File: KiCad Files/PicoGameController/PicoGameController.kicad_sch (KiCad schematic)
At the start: 26 parts, among them J1 USB_OTG, J2 Conn_01x02, U1 RP2040, U2 NCP1117-3.3_SOT223, U3 W25Q128JVS, Y1 ABLS-12.000MHZ-B4-T

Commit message: Adding lots of buttons
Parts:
- added C17, C18, C19, C20: 1uF, symbol Device:C
- added R2, R6, R7, R8: 10k, symbol Device:R
- added SW1, SW10, SW11, SW12, SW13, SW2, SW3, SW4, SW5, SW6, SW7, SW8, SW9: SW_SPST, symbol Switch:SW_SPST
- added T1, T2: THB001P, symbol CustomParts:THB001P
- added U4, U5: DRV2605LDGS, Package_SO:VSSOP-10_3x3mm_P0.5mm, symbol Driver_Haptic:DRV2605LDGS
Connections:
- net GND: now also U1.57 (GND), C17.2, C18.1, C19.2, C20.2, SW1.2 (B), SW10.2 (B), SW11.2 (B), SW12.2 (B), SW13.2 (B), SW2.2 (B), SW3.2 (B), SW4.2 (B), SW5.2 (B), SW6.2 (B), SW7.2 (B), SW8.2 (B), SW9.2 (B), T1.1 (GND), T1.4 (GND), T1.7 (GND), T2.1 (GND), T2.4 (GND), T2.7 (GND), U4.8 (GND), U5.8 (GND)
- net QSPI_SCLK: now also U1.52 (QSPI_SCLK)
- net QSPI_SD0: now also U1.53 (QSPI_SD0)
- net QSPI_SD1: now also U1.55 (QSPI_SD1)
- net QSPI_SD2: now also U1.54 (QSPI_SD2)
- net QSPI_SD3: now also U1.51 (QSPI_SD3)
- net QSPI_SS: now also U1.56 (QSPI_SS)
- net XIN: now also U1.20 (XIN)
- net XOUT: now also U1.21 (XOUT)
- net LOGO: now reaches U1.14 (GPIO11)
- net LOGO: now also SW11.1 (A)
- net START: now reaches U1.15 (GPIO12)
- net START: now also SW3.1 (A)
- net SELECT: now reaches U1.16 (GPIO13)
- net SELECT: now also SW4.1 (A)
- net R1: now reaches U1.17 (GPIO14)
- net R1: now also SW7.1 (A)
- net L1: now reaches U1.18 (GPIO15)
- net L1: now also SW8.1 (A)
- net HAPTIC_L_SDA: now reaches U1.2 (GPIO0)
- net HAPTIC_L_SDA: now also R2.1
- net Y: now reaches U1.27 (GPIO16)
- net Y: now also SW13.1 (A)
- net X: now reaches U1.28 (GPIO17)
- net X: now also SW12.1 (A)
- net D_Up: now reaches U1.29 (GPIO18)
- net D_Up: now also SW1.1 (A)
- net HAPTIC_L_SCL: now reaches U1.3 (GPIO1)
- net HAPTIC_L_SCL: now also R6.1
- net D_Right: now reaches U1.30 (GPIO19)
- net D_Right: now also SW6.1 (A)
- net D_Left: now reaches U1.31 (GPIO20)
- net D_Left: now also SW5.1 (A)
- net D_Down: now reaches U1.32 (GPIO21)
- net D_Down: now also SW2.1 (A)
- net B: now reaches U1.34 (GPIO22)
- net B: now also SW10.1 (A)
- net A: now reaches U1.35 (GPIO23)
- net A: now also SW9.1 (A)
- net R3: now reaches U1.36 (GPIO24)
- net R3: now also T2.8 (Select)
- net L3: now reaches U1.37 (GPIO25)
- net L3: now also T1.8 (Select)
- net Lx: now reaches U1.38 (GPIO26_ADC0)
- net Lx: now also T1.3 (X)
- net Ly: now reaches U1.39 (GPIO27_ADC1)
- net Ly: now also T1.6 (Y)
- net HAPTIC_R_SDA: now reaches U1.4 (GPIO2)
- net HAPTIC_R_SDA: now also R7.1
- net Rx: now reaches U1.40 (GPIO28_ADC2)
- net Rx: now also T2.3 (X)
- net Ry: now reaches U1.41 (GPIO29_ADC3)
- net Ry: now also T2.6 (Y)
- net HAPTIC_R_SCL: now reaches U1.5 (GPIO3)
- net HAPTIC_R_SCL: now also R8.1
- new net: R8.2, U5.2 (SCL)
- new net: R6.2, U4.2 (SCL)
- new net: R7.2, U5.3 (SDA)
- new net: C19.1, U4.1 (REG)
- new net: R2.2, U4.3 (SDA)
- new net: C20.1, U5.1 (REG)
- new net +5V: C17.1, C18.2, T1.2 (VCC), T1.5 (VCC), T2.2 (VCC), T2.5 (VCC), U4.10 (VDD), U4.5 (EN), U5.10 (VDD), U5.5 (EN)
- no-connect marks 1 -> 5
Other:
- moved on the sheet: C2, C3, C5, J2, R1, R5, U3, Y1

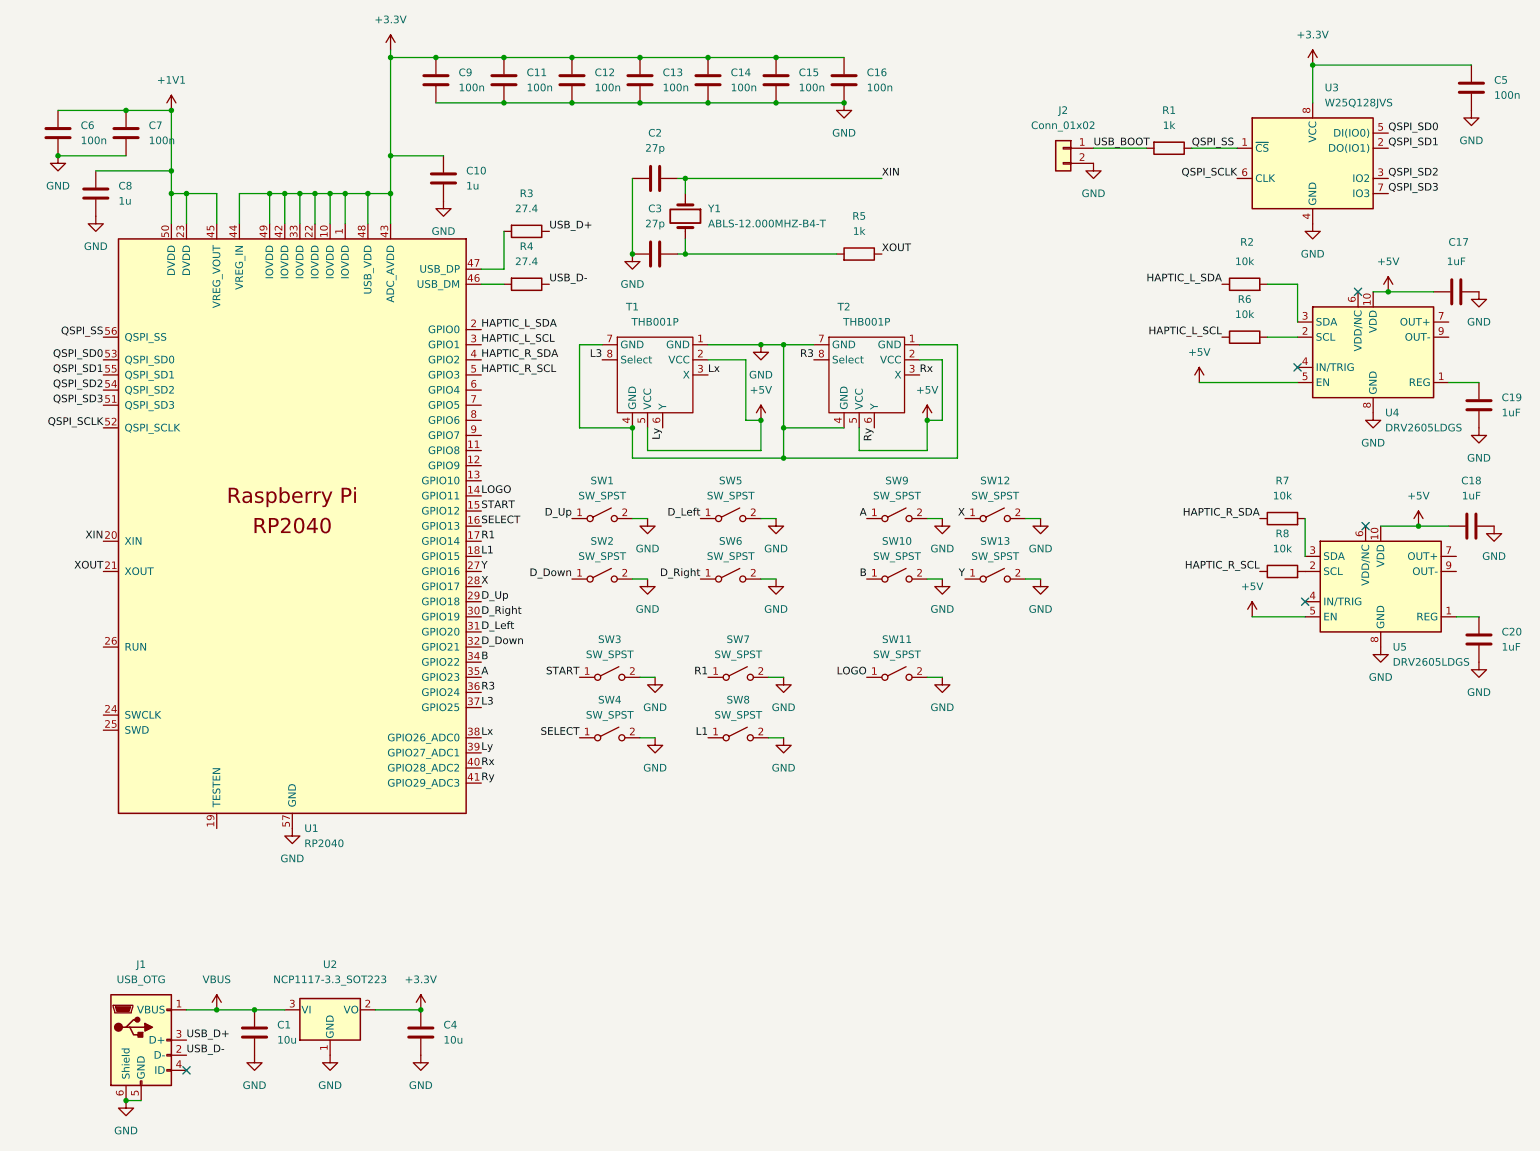
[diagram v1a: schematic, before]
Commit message: adding more ADCs
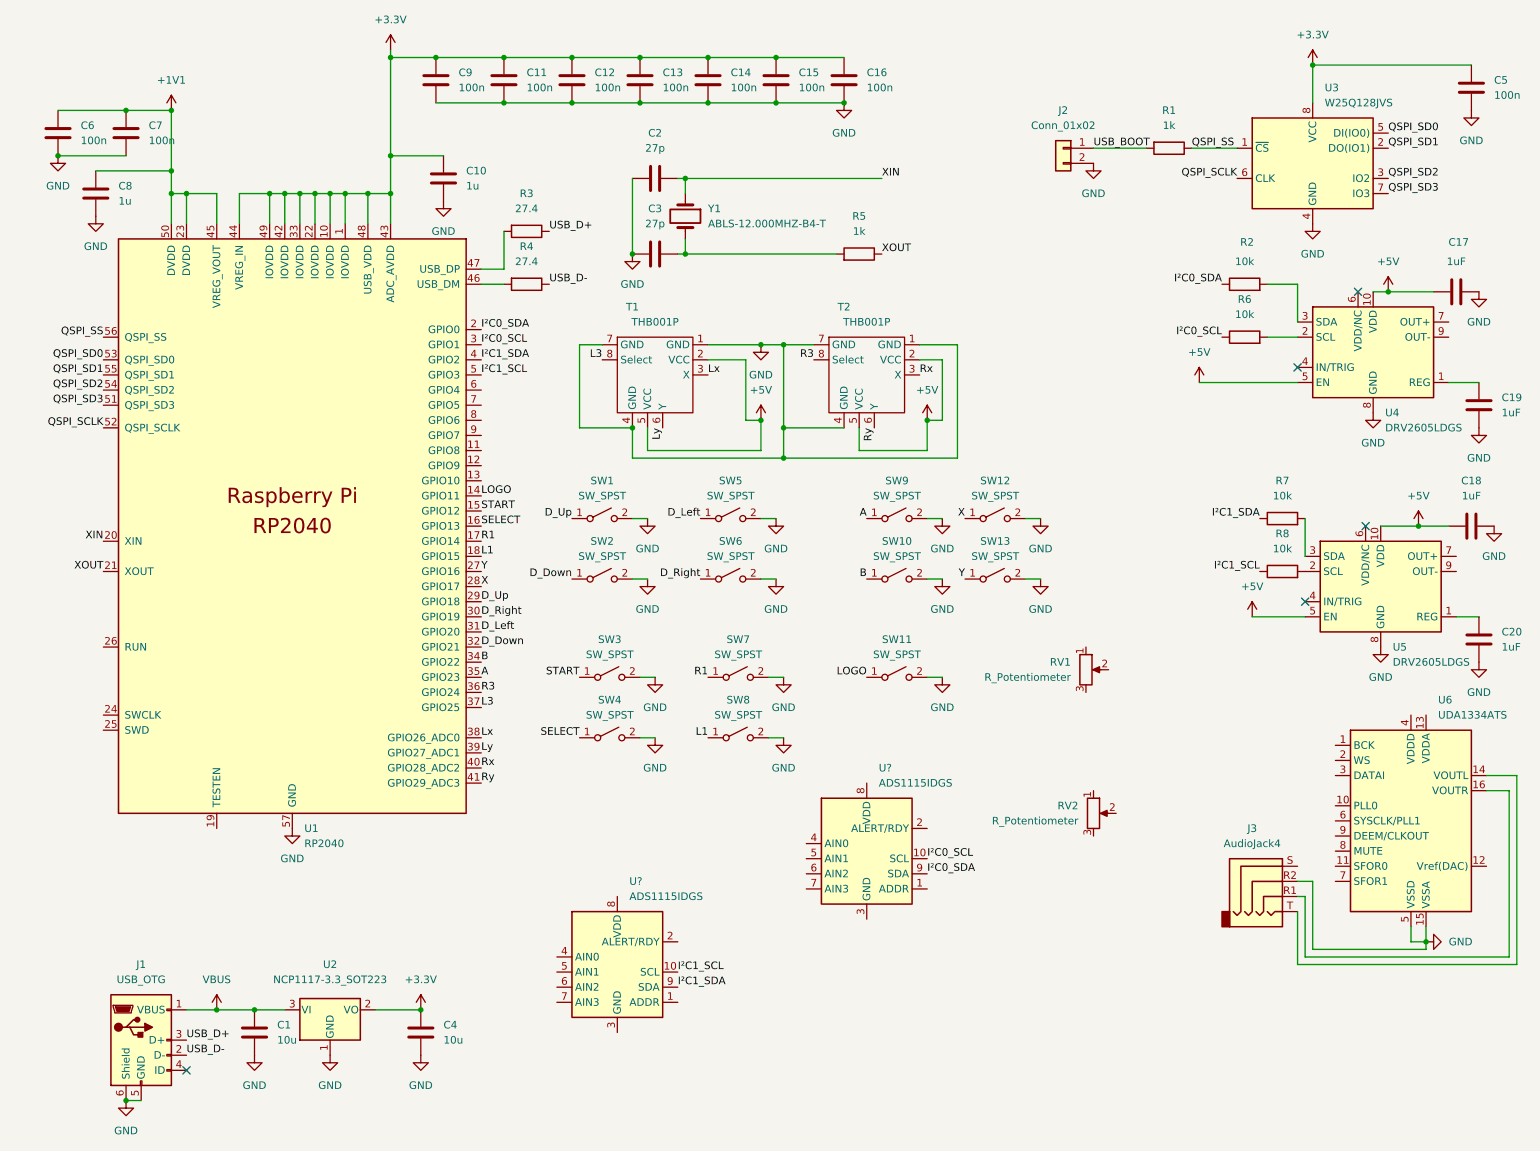
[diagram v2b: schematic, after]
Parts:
- added J3: AudioJack4, symbol Connector:AudioJack4
- added RV1, RV2: R_Potentiometer, symbol Device:R_Potentiometer
- added U6: UDA1334ATS, Package_SO:SSOP-16_4.4x5.2mm_P0.65mm, symbol Audio:UDA1334ATS
- added U? (x2): ADS1115IDGS, Package_SO:TSSOP-10_3x3mm_P0.5mm, symbol Analog_ADC:ADS1115IDGS
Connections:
- net GND: now also J3.R2, U6.15 (VSSA), U6.5 (VSSD)
- net HAPTIC_L_SCL renamed I²C0_SCL
- net I²C0_SCL: now also U?.10 (SCL)
- net HAPTIC_L_SDA renamed I²C0_SDA
- net I²C0_SDA: now also U?.9 (SDA)
- net HAPTIC_R_SCL renamed I²C1_SCL
- net I²C1_SCL: now also U?.10 (SCL)
- net HAPTIC_R_SDA renamed I²C1_SDA
- net I²C1_SDA: now also U?.9 (SDA)
- new net: J3.R1, U6.16 (VOUTR)
- new net: J3.T, U6.14 (VOUTL)

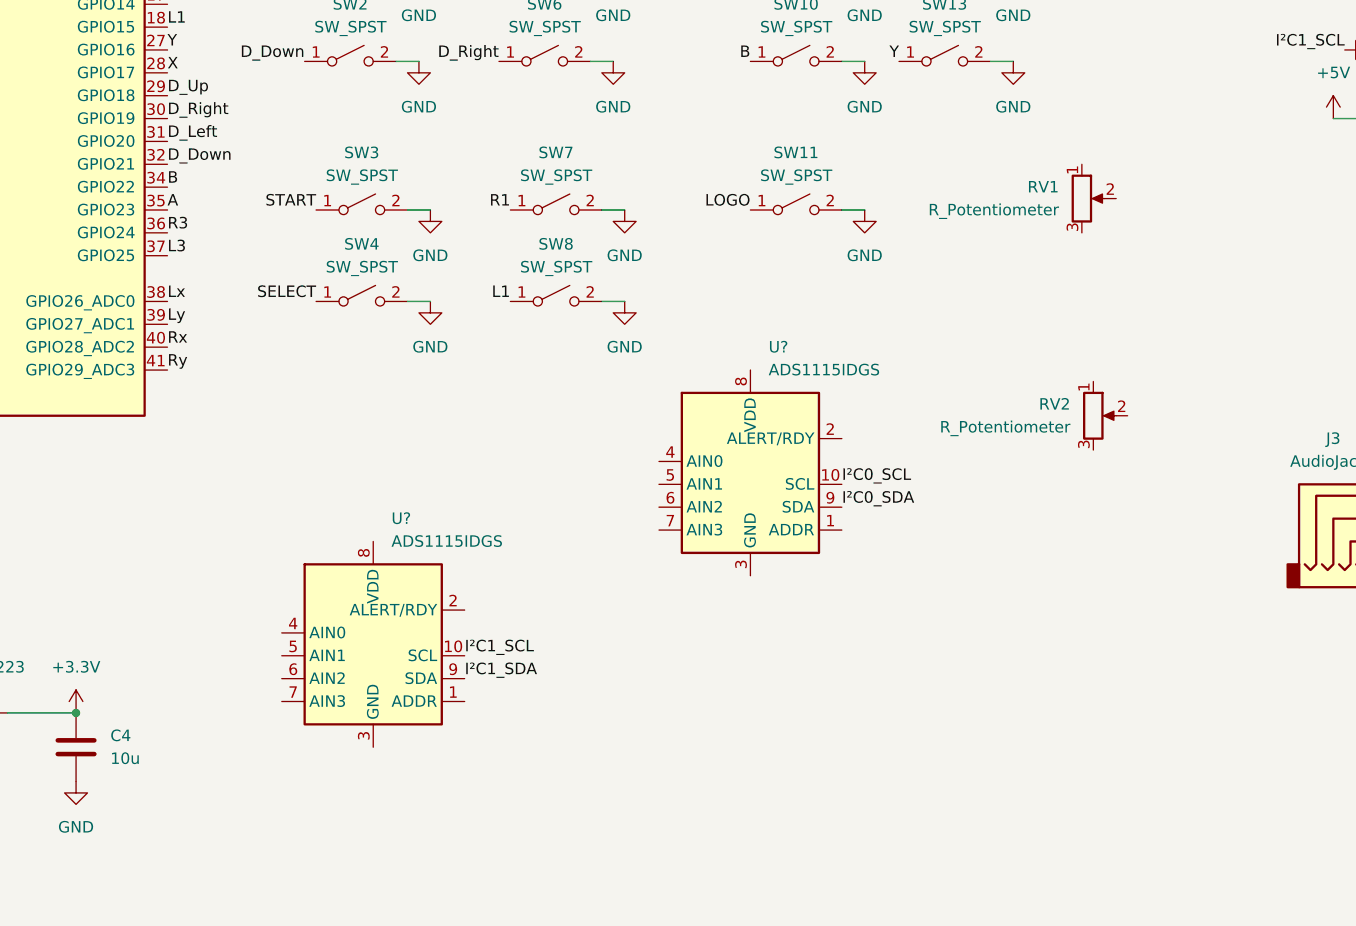
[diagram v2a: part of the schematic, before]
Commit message: Adding part footprints
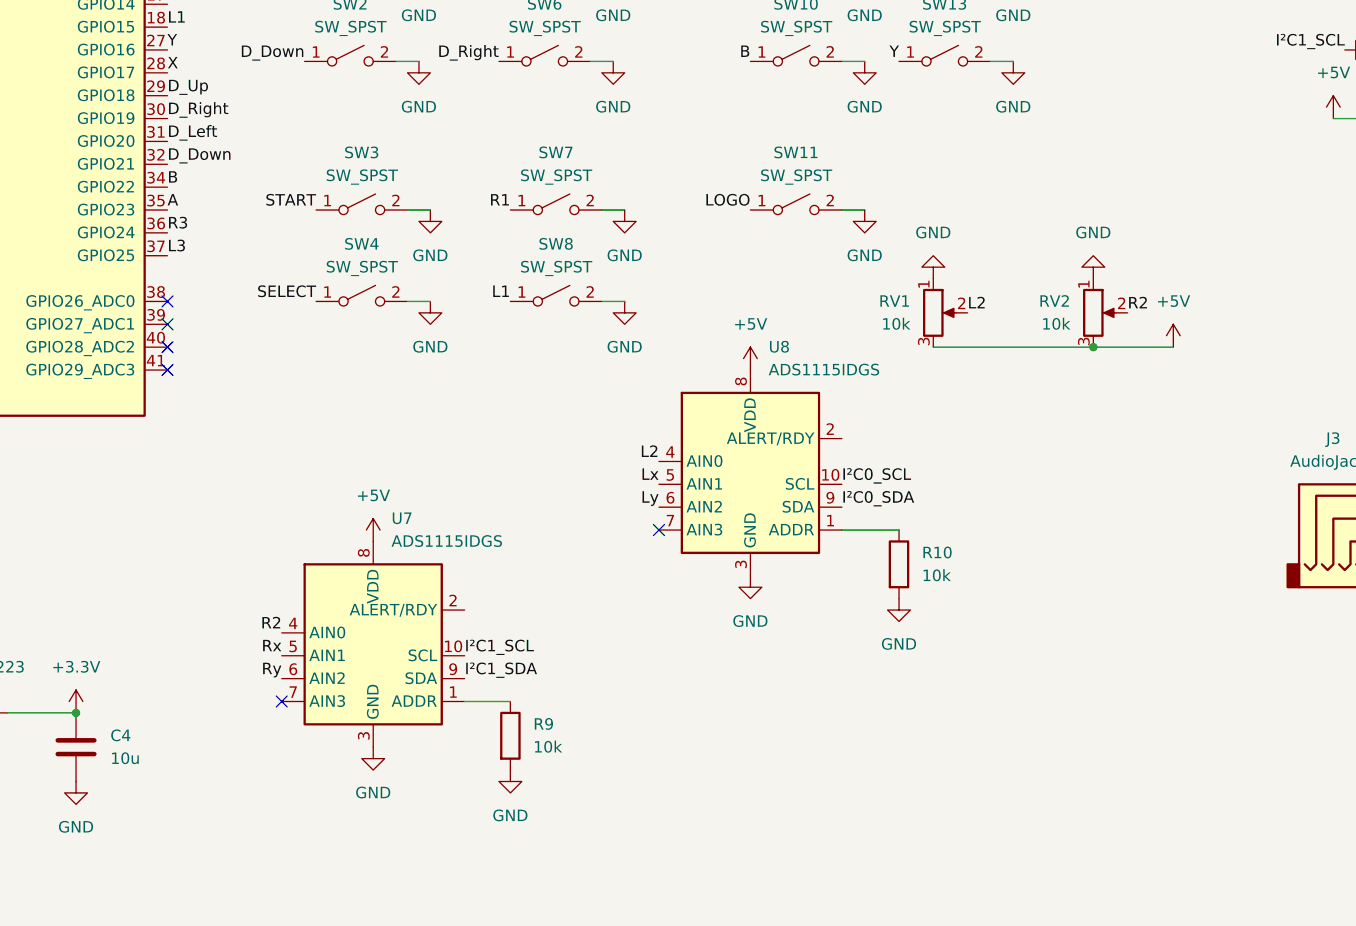
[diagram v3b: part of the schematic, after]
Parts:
- added R10, R9: 10k, Resistor_SMD:R_0201_0603Metric, symbol Device:R
- C1, C4: footprint (none) -> Capacitor_SMD:C_0402_1005Metric
- C10, C11, C12, C13, C14, C15, C16, C17, C18, C19, C2, C20, C3, C5, C6, C7, C8, C9: footprint (none) -> Capacitor_SMD:C_0201_0603Metric
- R1, R2, R5, R6, R7, R8: footprint (none) -> Resistor_SMD:R_0201_0603Metric
- R3, R4: footprint (none) -> Resistor_SMD:R_0402_1005Metric
- RV1, RV2: value R_Potentiometer -> 10k; footprint (none) -> Resistor_SMD:R_0201_0603Metric
- gave numbers to parts that had none: 2
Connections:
- net +5V: now also RV1.3, RV2.3, U7.8 (VDD), U8.8 (VDD)
- net GND: now also RV1.1, RV2.1, U7.3 (GND), U8.3 (GND), R10.2, R9.2
- net Lx: now also U8.5 (AIN1); no longer U1.38 (GPIO26_ADC0)
- net Ly: now also U8.6 (AIN2); no longer U1.39 (GPIO27_ADC1)
- net Rx: now also U7.5 (AIN1); no longer U1.40 (GPIO28_ADC2)
- net Ry: now also U7.6 (AIN2); no longer U1.41 (GPIO29_ADC3)
- net at U8.1 (ADDR): now also R10.1
- net L2: now reaches U8.4 (AIN0)
- net L2: now also RV1.2
- net R2: now reaches RV2.2
- net R2: now also U7.4 (AIN0)
- net at U7.1 (ADDR): now also R9.1
- no-connect marks 5 -> 11
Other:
- moved on the sheet: RV1, RV2
